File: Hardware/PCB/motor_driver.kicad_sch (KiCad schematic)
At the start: 6 parts, among them J1 Motor Power, J2 Conn_02x08_Odd_Even, U4 VNH5019ATR-E

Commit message: added a lot of stuff, going to work on LCD + Touch next
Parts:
- removed J2: Conn_02x08_Odd_Even, Connector_PinHeader_2.54mm:PinHeader_2x08_P2.54mm_Vertical, symbol Connector_Generic:Conn_02x08_Odd_Even
- removed U4: VNH5019ATR-E, Package_SO:ST_MultiPowerSO-30, symbol Driver_Motor:VNH5019A-E
- added J6: Brushed Motor Coil, TerminalBlock_CUI:TerminalBlock_CUI_TB007-508-02_1x02_P5.08mm_Horizontal, symbol Connector:Screw_Terminal_01x02
- added R5: 18k, Resistor_SMD:R_1206_3216Metric_Pad1.30x1.75mm_HandSolder, symbol Device:R_Small
- added U8: DRV8871DDA, Package_SO:Texas_HTSOP-8-1EP_3.9x4.9mm_P1.27mm_EP2.95x4.9mm_Mask2.4x3.1mm_ThermalVias, symbol Driver_Motor:DRV8871DDA
- C7: value 470u -> 22uF
- C8: value 0.1u -> 0.1uF
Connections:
- net Vdrive: now also U8.5 (VM)
- net GNDPWR renamed GND2
- net GND2: now also R5.2, U8.1 (GND), U8.7 (GND), U8.9 (GND)
- new net: R5.1, U8.4 (ILIM)
- new net: J6.1 (Pin_1), U8.6 (OUT1)
- new net: J6.2 (Pin_2), U8.8 (OUT2)
- new net IN1: U8.3 (IN1)
- new net IN2: U8.2 (IN2)
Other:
- note added: "6.5V - 45V"
- moved on the sheet: C7, C8, J1, NT1

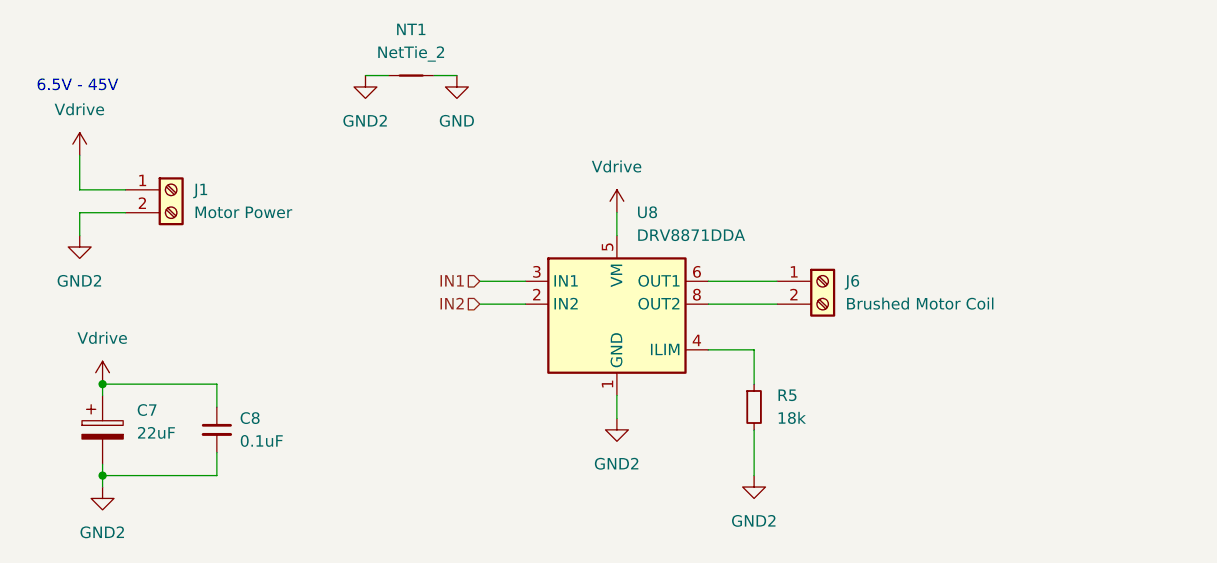
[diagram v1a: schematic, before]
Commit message: Added brushless DC support, fixed terminal blocks too
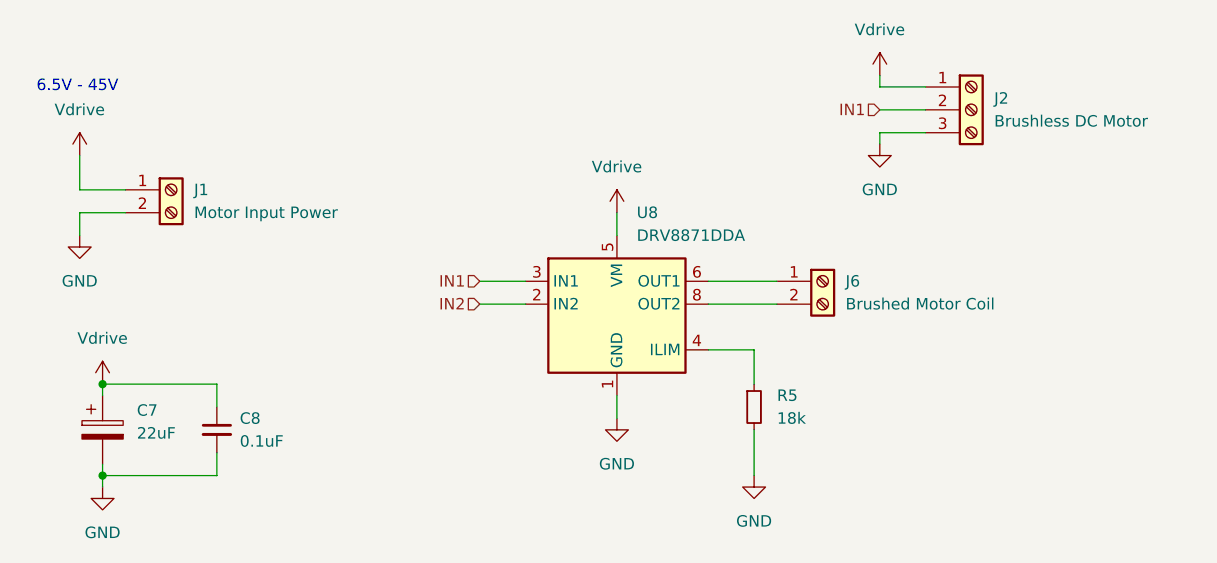
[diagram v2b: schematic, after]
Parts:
- removed NT1: NetTie_2, symbol Device:NetTie_2
- added J2: Brushless DC Motor, Vendor_Footprints:CONN_1-2834011-3_TEC, symbol Connector:Screw_Terminal_01x03
- C7: footprint Capacitor_THT:CP_Radial_D10.0mm_P5.00mm -> Capacitor_SMD:CP_Elec_8x10; DigiKey Link (none) -> https://www.digikey.com/en/products/detail/nichicon/UUX2A22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; MPN ECA-1HM471 -> UUX2A220MNL6GS; Manufacturer (none) -> Nichicon
- C8: footprint Capacitor_SMD:C_0603_1608Metric_Pad1.08x0.95mm_HandSolder -> Capacitor_SMD:C_1206_3216Metric_Pad1.33x1.80mm_HandSolder; DigiKey Link (none) -> https://www.digikey.com/en/products/detail/samsung-electro-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; MPN GCM188R71H104KA57J -> CL31B104KEHSFNE; Manufacturer (none) -> Samsung Electro-Mechanics
- J1: value Motor Power -> Motor Input Power; footprint TerminalBlock_CUI:TerminalBlock_CUI_TB007-508-02_1x02_P5.08mm_Horizontal -> Vendor_Footprints:CONN2_1-2834011-2_TEC; DigiKey Link (none) -> https://www.digikey.com/en/products/detail/te-connectivity-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; MPN (none) -> 1-2834011-2; Manufacturer (none) -> TE Connectivity AMP Connectors
- J6: footprint TerminalBlock_CUI:TerminalBlock_CUI_TB007-508-02_1x02_P5.08mm_Horizontal -> Vendor_Footprints:CONN2_1-2834011-2_TEC; DigiKey Link (none) -> https://www.digikey.com/en/products/detail/te-connectivity-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; MPN (none) -> 1-2834011-2; Manufacturer (none) -> TE Connectivity AMP Connectors
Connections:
- net GND2 is gone; now on net GND: C7.2, C8.2, J1.2 (Pin_2), R5.2, U8.1 (GND), U8.7 (GND), U8.9 (GND)
- net GND: now also J2.3 (Pin_3)
- net IN1: now also J2.2 (Pin_2)
- net Vdrive: now also J2.1 (Pin_1)

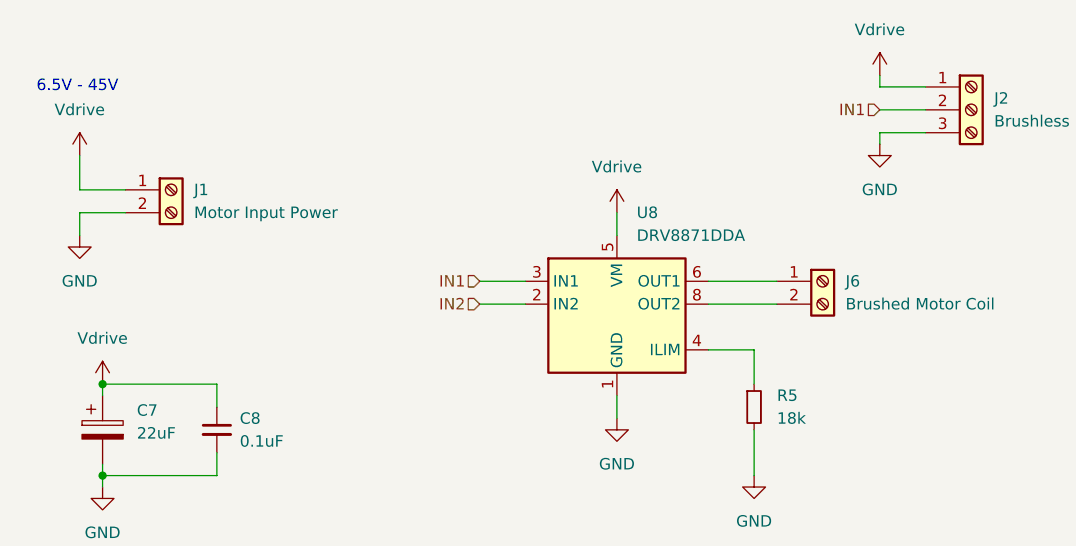
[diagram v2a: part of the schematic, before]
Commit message: switched to making buck converter to save costs and space, and to allow for LDO after 5.5V for better stability
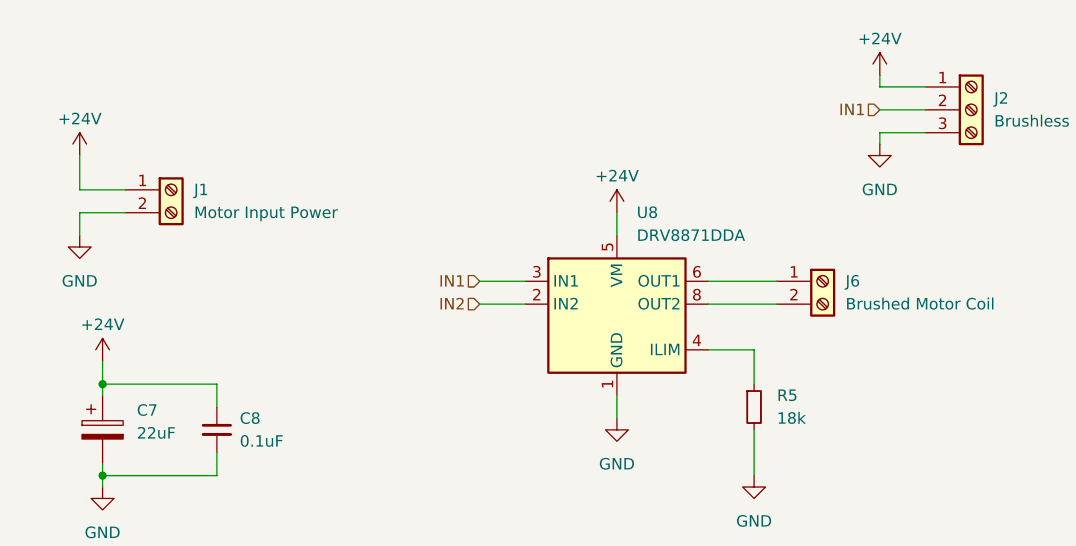
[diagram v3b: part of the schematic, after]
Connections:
- net Vdrive renamed +24V
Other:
- note removed: "6.5V - 45V"
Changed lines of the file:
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@@
 	(paper "A5")
+	(junction
+		(at 54.61 73.66)
+		(diameter 0)
+		(color 0 0 0 0)
+	)
 	(junction
 		(at 54.61 63.5)
@@
 		(color 0 0 0 0)
 	)
-	(junction
-		(at 54.61 73.66)
-		(diameter 0)
-		(color 0 0 0 0)
-	)
 	(wire
 		(pts
@@
 	(wire
 		(pts
+			(xy 54.61 60.96) (xy 54.61 63.5)
+		)
+		(stroke
+			(width 0)
+			(type default)
+		)
+	)
+	(wire
+		(pts
 			(xy 52.07 44.45) (xy 57.15 44.45)
 		)
@@
 			(width 0)
 			(type default)
-		)
-	)
-	(text "6.5V - 45V"
-		(exclude_from_sim no)
-		(at 51.816 30.48 0)
-		(effects
-			(font
-				(size 1.27 1.27)
-			)
 		)
 	)
@@
 	)
 	(symbol
-		(lib_id "power:Vdrive")
-		(at 140.97 29.21 0)
+		(lib_id "power:+24V")
+		(at 54.61 60.96 0)
 		(unit 1)
 		(exclude_from_sim no)
@@
 		(on_board yes)
 		(dnp no)
-		(fields_autoplaced yes)
-		(property "Reference" "#PWR011"
-			(at 140.97 33.02 0)
-			(effects
-				(font
-					(size 1.27 1.27)
-				)
-				(hide yes)
-			)
-		)
-		(property "Value" "Vdrive"
-			(at 140.97 24.13 0)
+		(property "Reference" "#PWR013"
+			(at 54.61 64.77 0)
+			(effects
+				(font
+					(size 1.27 1.27)
+				)
+				(hide yes)
+			)
+		)
+		(property "Value" "+24V"
+			(at 54.61 56.896 0)
 			(effects
 				(font
@@
 		)
 		(property "Footprint" ""
-			(at 140.97 29.21 0)
+			(at 54.61 60.96 0)
 			(effects
 				(font
@@
 		)
 		(property "Datasheet" ""
-			(at 140.97 29.21 0)
-			(effects
-				(font
-					(size 1.27 1.27)
-				)
-				(hide yes)
-			)
-		)
-		(property "Description" "Power symbol creates a global label with name \"Vdrive\""
-			(at 140.97 29.21 0)
+			(at 54.61 60.96 0)
+			(effects
+				(font
+					(size 1.27 1.27)
+				)
+				(hide yes)
+			)
+		)
+		(property "Description" "Power symbol creates a global label with name \"+24V\""
+			(at 54.61 60.96 0)
 			(effects
 				(font
@@
 			(project "PCB"
 				(path "/c3756407-a933-418d-a16a-ea4e5b091ef7/ac699c2b-014c-4302-987d-d1905114f179"
-					(reference "#PWR011")
+					(reference "#PWR013")
 					(unit 1)
 				)
@@
 	)
 	(symbol
-		(lib_id "power:Vdrive")
-		(at 111.76 44.45 0)
-		(unit 1)
-		(exclude_from_sim no)
-		(in_bom yes)
-		(on_board yes)
-		(dnp no)
-		(fields_autoplaced yes)
-		(property "Reference" "#PWR015"
-			(at 111.76 48.26 0)
-			(effects
-				(font
-					(size 1.27 1.27)
-				)
-				(hide yes)
-			)
-		)
-		(property "Value" "Vdrive"
-			(at 111.76 39.37 0)
-			(effects
-				(font
-					(size 1.27 1.27)
-				)
-			)
-		)
-		(property "Footprint" ""
-			(at 111.76 44.45 0)
-			(effects
-				(font
-					(size 1.27 1.27)
-				)
-				(hide yes)
-			)
-		)
-		(property "Datasheet" ""
-			(at 111.76 44.45 0)
-			(effects
-				(font
-					(size 1.27 1.27)
-				)
-				(hide yes)
-			)
-		)
-		(property "Description" "Power symbol creates a global label with name \"Vdrive\""
-			(at 111.76 44.45 0)
-			(effects
-				(font
-					(size 1.27 1.27)
-				)
-				(hide yes)
-			)
-		)
-		(pin "1"
-		)
-		(instances
-			(project "PCB"
-				(path "/c3756407-a933-418d-a16a-ea4e5b091ef7/ac699c2b-014c-4302-987d-d1905114f179"
-					(reference "#PWR015")
-					(unit 1)
-				)
-			)
-		)
-	)
-	(symbol
 		(lib_id "Connector:Screw_Terminal_01x03")
 		(at 151.13 33.02 0)
@@
 	)
 	(symbol
+		(lib_id "power:+24V")
+		(at 111.76 44.45 0)
+		(unit 1)
+		(exclude_from_sim no)
+		(in_bom yes)
+		(on_board yes)
+		(dnp no)
+		(property "Reference" "#PWR015"
+			(at 111.76 48.26 0)
+			(effects
+				(font
+					(size 1.27 1.27)
+				)
+				(hide yes)
+			)
+		)
+		(property "Value" "+24V"
+			(at 111.76 40.386 0)
+			(effects
+				(font
+					(size 1.27 1.27)
+				)
+			)
+		)
+		(property "Footprint" ""
+			(at 111.76 44.45 0)
+			(effects
+				(font
+					(size 1.27 1.27)
+				)
+				(hide yes)
+			)
+		)
+		(property "Datasheet" ""
+			(at 111.76 44.45 0)
+			(effects
+				(font
+					(size 1.27 1.27)
+				)
+				(hide yes)
+			)
+		)
+		(property "Description" "Power symbol creates a global label with name \"+24V\""
+			(at 111.76 44.45 0)
+			(effects
+				(font
+					(size 1.27 1.27)
+				)
+				(hide yes)
+			)
+		)
+		(pin "1"
+		)
+		(instances
+			(project "PCB"
+				(path "/c3756407-a933-418d-a16a-ea4e5b091ef7/ac699c2b-014c-4302-987d-d1905114f179"
+					(reference "#PWR015")
+					(unit 1)
+				)
+			)
+		)
+	)
+	(symbol
 		(lib_id "power:GND")
 		(at 140.97 36.83 0)
@@
 	)
 	(symbol
+		(lib_id "power:+24V")
+		(at 52.07 38.1 0)
+		(unit 1)
+		(exclude_from_sim no)
+		(in_bom yes)
+		(on_board yes)
+		(dnp no)
+		(property "Reference" "#PWR069"
+			(at 52.07 41.91 0)
+			(effects
+				(font
+					(size 1.27 1.27)
+				)
+				(hide yes)
+			)
+		)
+		(property "Value" "+24V"
+			(at 52.07 34.036 0)
+			(effects
+				(font
+					(size 1.27 1.27)
+				)
+			)
+		)
+		(property "Footprint" ""
+			(at 52.07 38.1 0)
+			(effects
+				(font
+					(size 1.27 1.27)
+				)
+				(hide yes)
+			)
+		)
+		(property "Datasheet" ""
+			(at 52.07 38.1 0)
+			(effects
+				(font
+					(size 1.27 1.27)
+				)
+				(hide yes)
+			)
+		)
+		(property "Description" "Power symbol creates a global label with name \"+24V\""
+			(at 52.07 38.1 0)
+			(effects
+				(font
+					(size 1.27 1.27)
+				)
+				(hide yes)
+			)
+		)
+		(pin "1"
+		)
+		(instances
+			(project ""
+				(path "/c3756407-a933-418d-a16a-ea4e5b091ef7/ac699c2b-014c-4302-987d-d1905114f179"
+					(reference "#PWR069")
+					(unit 1)
+				)
+			)
+		)
+	)
+	(symbol
 		(lib_id "power:GND")
 		(at 54.61 74.93 0)
@@
 				(path "/c3756407-a933-418d-a16a-ea4e5b091ef7/ac699c2b-014c-4302-987d-d1905114f179"
 					(reference "#PWR012")
-					(unit 1)
-				)
-			)
-		)
-	)
-	(symbol
-		(lib_id "power:Vdrive")
-		(at 54.61 63.5 0)
-		(unit 1)
-		(exclude_from_sim no)
-		(in_bom yes)
-		(on_board yes)
-		(dnp no)
-		(fields_autoplaced yes)
-		(property "Reference" "#PWR013"
-			(at 54.61 67.31 0)
-			(effects
-				(font
-					(size 1.27 1.27)
-				)
-				(hide yes)
-			)
-		)
-		(property "Value" "Vdrive"
-			(at 54.61 58.42 0)
-			(effects
-				(font
-					(size 1.27 1.27)
-				)
-			)
-		)
-		(property "Footprint" ""
-			(at 54.61 63.5 0)
-			(effects
-				(font
-					(size 1.27 1.27)
-				)
-				(hide yes)
-			)
-		)
-		(property "Datasheet" ""
-			(at 54.61 63.5 0)
-			(effects
-				(font
-					(size 1.27 1.27)
-				)
-				(hide yes)
-			)
-		)
-		(property "Description" "Power symbol creates a global label with name \"Vdrive\""
-			(at 54.61 63.5 0)
-			(effects
-				(font
-					(size 1.27 1.27)
-				)
-				(hide yes)
-			)
-		)
-		(pin "1"
-		)
-		(instances
-			(project "PAC"
-				(path "/c3756407-a933-418d-a16a-ea4e5b091ef7/ac699c2b-014c-4302-987d-d1905114f179"
-					(reference "#PWR013")
 					(unit 1)
 				)
@@
 	)
 	(symbol
-		(lib_id "power:Vdrive")
-		(at 52.07 38.1 0)
+		(lib_id "power:+24V")
+		(at 140.97 29.21 0)
 		(unit 1)
 		(exclude_from_sim no)
@@
 		(on_board yes)
 		(dnp no)
-		(fields_autoplaced yes)
-		(property "Reference" "#PWR09"
-			(at 52.07 41.91 0)
-			(effects
-				(font
-					(size 1.27 1.27)
-				)
-				(hide yes)
-			)
-		)
-		(property "Value" "Vdrive"
-			(at 52.07 33.02 0)
+		(property "Reference" "#PWR011"
+			(at 140.97 33.02 0)
+			(effects
+				(font
+					(size 1.27 1.27)
+				)
+				(hide yes)
+			)
+		)
+		(property "Value" "+24V"
+			(at 140.97 25.146 0)
 			(effects
 				(font
@@
 		)
 		(property "Footprint" ""
-			(at 52.07 38.1 0)
+			(at 140.97 29.21 0)
 			(effects
 				(font
@@
 		)
 		(property "Datasheet" ""
-			(at 52.07 38.1 0)
-			(effects
-				(font
-					(size 1.27 1.27)
-				)
-				(hide yes)
-			)
-		)
-		(property "Description" "Power symbol creates a global label with name \"Vdrive\""
-			(at 52.07 38.1 0)
+			(at 140.97 29.21 0)
+			(effects
+				(font
+					(size 1.27 1.27)
+				)
+				(hide yes)
+			)
+		)
+		(property "Description" "Power symbol creates a global label with name \"+24V\""
+			(at 140.97 29.21 0)
 			(effects
 				(font
@@
 		)
 		(instances
-			(project ""
+			(project "PCB"
 				(path "/c3756407-a933-418d-a16a-ea4e5b091ef7/ac699c2b-014c-4302-987d-d1905114f179"
-					(reference "#PWR09")
+					(reference "#PWR011")
 					(unit 1)
 				)

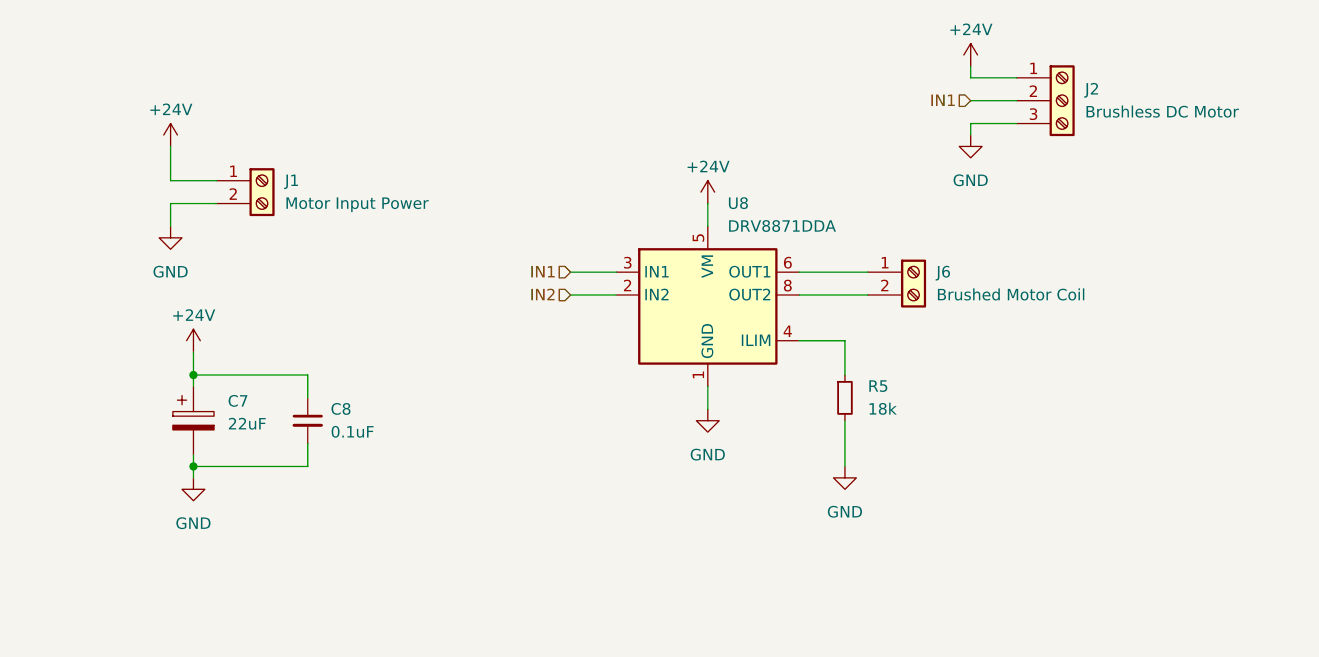
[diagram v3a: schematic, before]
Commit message: consolidated IO for LCD block, broke out hierarchial pins, need to start wiring everything up and then on to layout
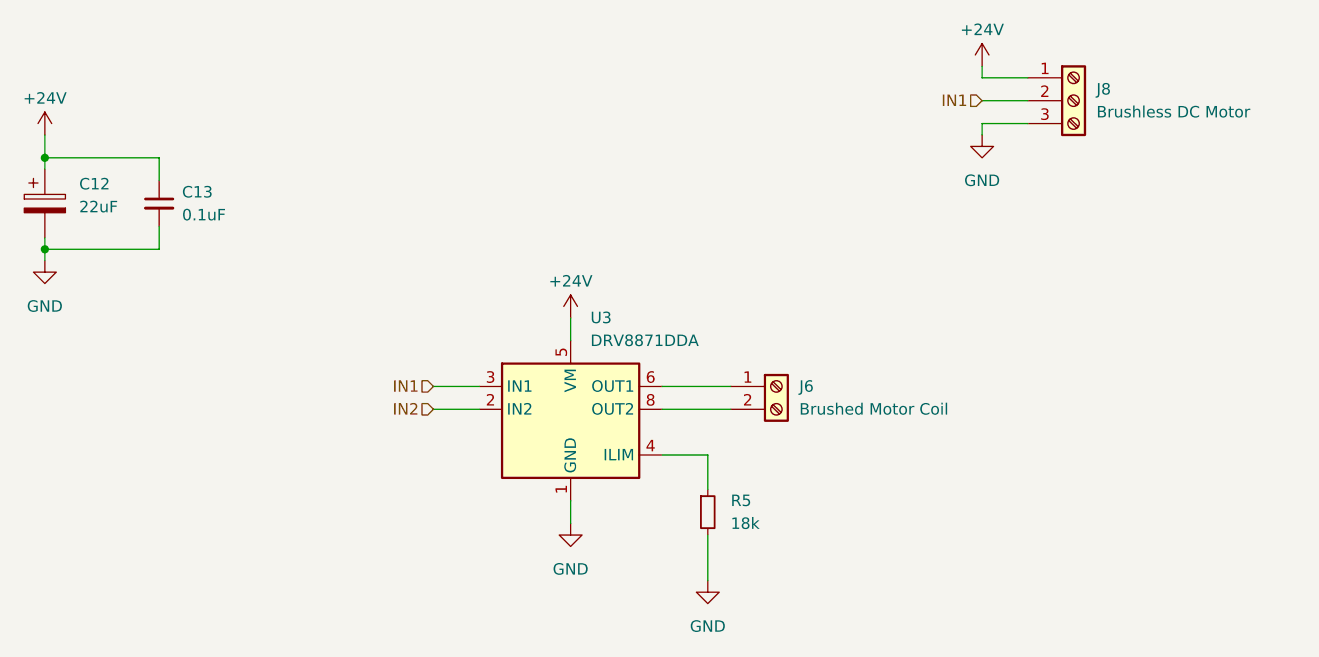
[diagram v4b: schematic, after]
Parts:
- removed J1: Motor Input Power, Vendor_Footprints:CONN2_1-2834011-2_TEC, symbol Connector:Screw_Terminal_01x02
- renumbered C7 to C12, C8 to C13, J2 to J8, U8 to U3
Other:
- moved on the sheet: C12, C13, J6, J8, R5, U3
